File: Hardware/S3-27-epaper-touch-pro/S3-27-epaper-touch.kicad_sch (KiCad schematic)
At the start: 102 parts, among them J1 AFC24-S24FIC-00, J10 Conn_01x06_Pin, J2 Conn_01x06, J3 Conn_01x06, J4 Conn_01x06_Female, J5 Groove sensor, J6 Conn_01x05_Pin, J7 Conn_01x04_Pin, J8 Conn_01x06, Q1 Si1308, Q2 Si2301, SW1 SW_Push, SW2 SW_Push, SW3 SW_Push, SW4 SW_Push, SW5 SW_Push, SW6 SW_Push, SW7 SW_Push, SW8 SW_Push, SW9 SW_Push, U1 ESP32-S3-WROOM-1-N8, U2 RT9013, U3 KoreanHropartsElecTYPE-C-31-M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, U5 BME680, U6 TPL5110, U7 RFM95W-868S2, U8 LSM6DSL

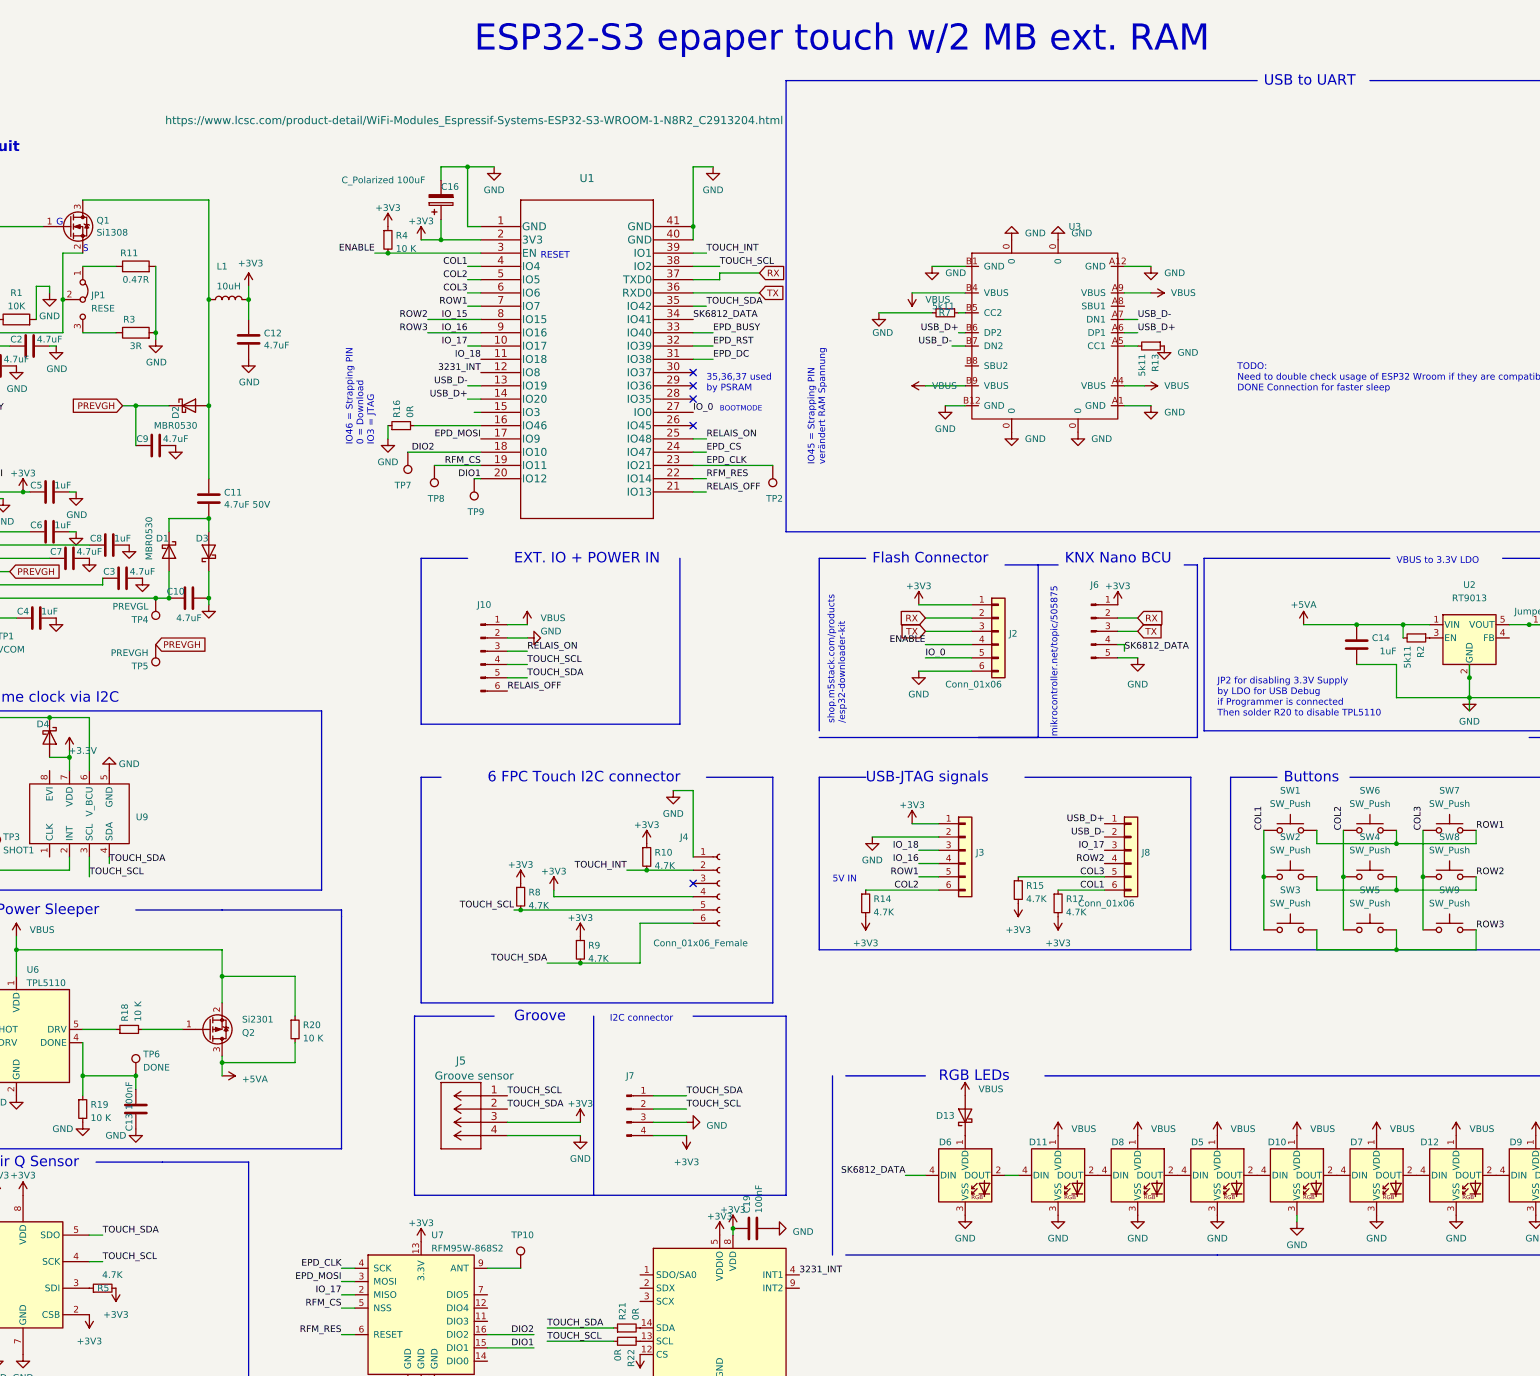
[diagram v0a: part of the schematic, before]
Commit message: Changed Footprint of BME680 and Silkscreen
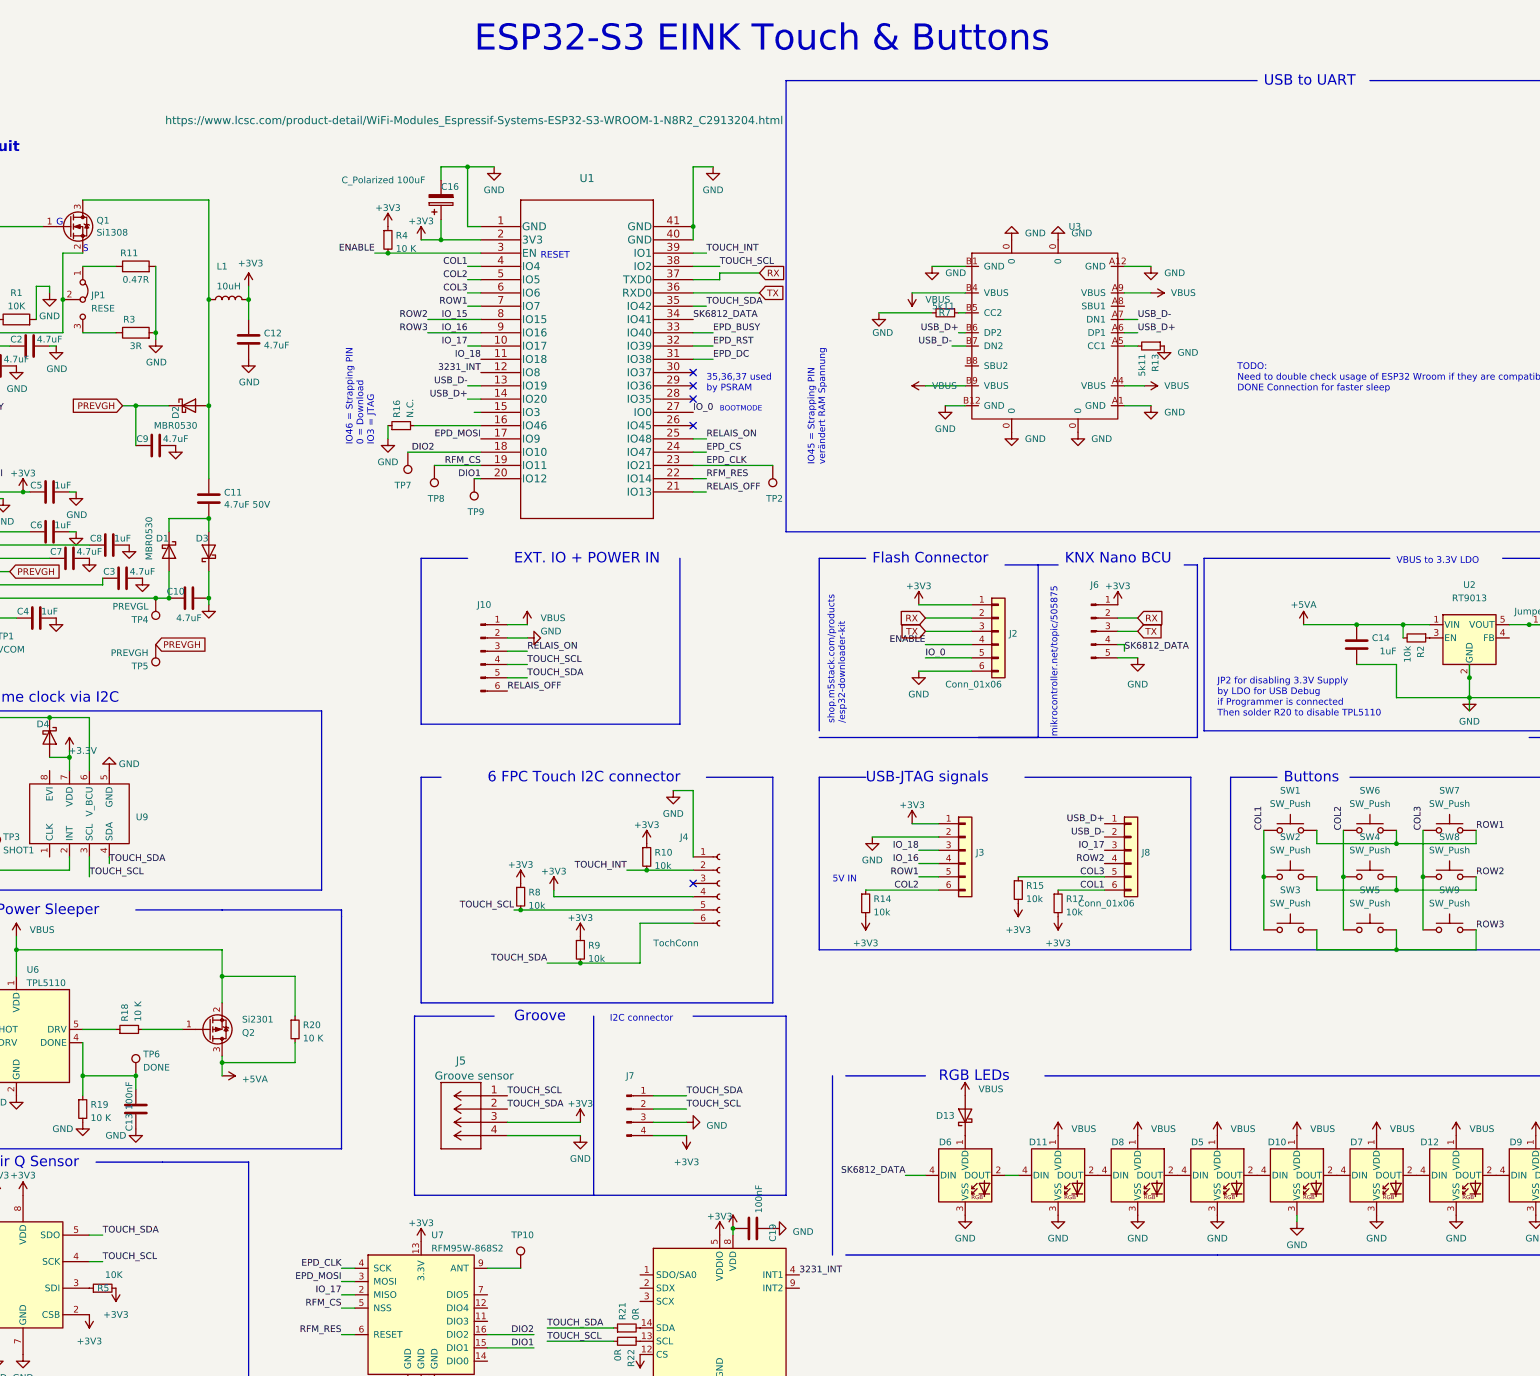
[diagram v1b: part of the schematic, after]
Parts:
- C11: LCSC C1779 -> C28323
- C13, C20: LCSC C28323 -> C49678
- C14, C15: footprint Capacitor_SMD:C_0805_2012Metric -> Capacitor_SMD:C_0805_2012Metric_Pad1.18x1.45mm_HandSolder
- C16: LCSC C129289 -> C28323
- J4: value Conn_01x06_Female -> TochConn
- L1: footprint footprint:SWPA4030S1R0NT -> tp4056:IND-SMD_L4.0-W4.0
- R10, R9: value 4.7K -> 10k; LCSC (none) -> C17414
- R12, R18, R19, R20, R4, R6: LCSC C25804 -> C17414
- R13, R7: LCSC C60816 -> C27834
- R14, R15, R17, R8: value 4.7K -> 10k; LCSC C23162 -> C17414
- R16: value 0R -> N.C.
- R2: value 5k11 -> 10k; LCSC C60816 -> C17414
- R21, R22: LCSC (none) -> C17477
- R5: value 4.7K -> 10K; LCSC C23162 -> C17414
- U5: footprint Package_LGA:Bosch_LGA-8_3x3mm_P0.8mm_ClockwisePinNumbering -> tp4056:LGA-8_L3.0-W3.0-P0.80-TR
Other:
- note added: "ESP32-S3 EINK Touch & Buttons"
- note removed: "ESP32-S3 epaper touch w/2 MB ext. RAM"
- title: ESP32-C3 epaper controller with touch -> ESP32-S3 EInk controller with touch
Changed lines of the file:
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@@
   (paper "A3")
   (title_block
-    (title "ESP32-C3 epaper controller with touch")
-    (date "2022-11-22")
-    (rev "1.1")
+    (title "ESP32-S3 EInk controller with touch")
+    (date "2023-03-07")
+    (rev "1.0")
     (comment 1 "be used in home appliances with no more than 200 Watts top consumption.")
     (comment 2 "industrial heavy load devices. This an experimental switch that should only")
     (comment 3 "it should NOT be used in any case for machinery that is for medical use or")
     (comment 4 "IMPORTANT: If used as an ON / OFF switch")
+    (comment 5 "NO Comercial USE. GPL LICENSE")
   )
   (junction (at 341.63 179.07) (diameter 0) (color 0 0 0 0)
@@
     (effects (font (size 1.27 1.27)) (justify left bottom))
   )
-  (text "ESP32-S3 epaper touch w/2 MB ext. RAM" (at 160.02 21.59 0)
+  (text "ESP32-S3 EINK Touch & Buttons" (at 160.02 21.59 0)
     (effects (font (size 5 5)) (justify left bottom))
   )
@@
       (effects (font (size 1.27 1.27)) (justify left))
     )
-    (property "Value" "4.7K" (at 170.4086 184.5822 0)
+    (property "Value" "10k" (at 170.4086 184.5822 0)
       (effects (font (size 1.27 1.27)) (justify left))
     )
@@
       (effects (font (size 1.27 1.27)) hide)
     )
-    (property "LCSC" "C23162" (at 168.91 182.88 0)
+    (property "LCSC" "C17414" (at 168.91 182.88 0)
       (effects (font (size 1.27 1.27)) hide)
     )
@@
       (effects (font (size 1.27 1.27)) hide)
     )
-    (property "LCSC" "" (at 189.23 265.43 0)
+    (property "LCSC" "C17477" (at 189.23 265.43 0)
       (effects (font (size 1.27 1.27)) hide)
     )
@@
       (effects (font (size 1.27 1.27)) hide)
     )
-    (property "LCSC" "C60816" (at 289.56 77.47 0)
+    (property "LCSC" "C27834" (at 289.56 77.47 0)
       (effects (font (size 1.27 1.27)) hide)
     )
@@
       (effects (font (size 1.27 1.27)) (justify left))
     )
-    (property "Value" "4.7K" (at 273.2786 185.8522 0)
+    (property "Value" "10k" (at 273.2786 185.8522 0)
       (effects (font (size 1.27 1.27)) (justify left))
     )
@@
       (effects (font (size 1.27 1.27)) hide)
     )
-    (property "LCSC" "C23162" (at 271.78 184.15 0)
+    (property "LCSC" "C17414" (at 271.78 184.15 0)
       (effects (font (size 1.27 1.27)) hide)
     )
@@
       (effects (font (size 1.27 1.27)) (justify left))
     )
-    (property "Value" "4.7K" (at 181.8386 194.7422 0)
+    (property "Value" "10k" (at 181.8386 194.7422 0)
       (effects (font (size 1.27 1.27)) (justify left))
     )
@@
       (effects (font (size 1.27 1.27)) hide)
     )
-    (property "LCSC" "" (at 180.34 193.04 0)
+    (property "LCSC" "C17414" (at 180.34 193.04 0)
       (effects (font (size 1.27 1.27)) hide)
     )
@@
       (effects (font (size 1.27 1.27)) (justify left))
     )
-    (property "Value" "4.7K" (at 194.5386 176.9622 0)
+    (property "Value" "10k" (at 194.5386 176.9622 0)
       (effects (font (size 1.27 1.27)) (justify left))
     )
@@
       (effects (font (size 1.27 1.27)) hide)
     )
-    (property "LCSC" "" (at 193.04 175.26 0)
+    (property "LCSC" "C17414" (at 193.04 175.26 0)
       (effects (font (size 1.27 1.27)) hide)
     )
@@
       (effects (font (size 1.27 1.27)) hide)
     )
-    (property "LCSC" "" (at 189.23 267.97 0)
+    (property "LCSC" "C17477" (at 189.23 267.97 0)
       (effects (font (size 1.27 1.27)) hide)
     )
@@
       (effects (font (size 1.27 1.27)) (justify left))
     )
-    (property "Value" "4.7K" (at 236.4486 185.8522 0)
+    (property "Value" "10k" (at 236.4486 185.8522 0)
       (effects (font (size 1.27 1.27)) (justify left))
     )
@@
       (effects (font (size 1.27 1.27)) hide)
     )
-    (property "LCSC" "C23162" (at 234.95 184.15 0)
+    (property "LCSC" "C17414" (at 234.95 184.15 0)
       (effects (font (size 1.27 1.27)) hide)
     )
@@
   (symbol (lib_id "Device:C") (at 213.36 246.38 270) (unit 1)
     (in_bom yes) (on_board yes) (dnp no)
-    (property "Reference" "C19" (at 212.1916 243.459 0)
+    (property "Reference" "C19" (at 217.17 248.92 0)
       (effects (font (size 1.27 1.27)) (justify right))
     )
@@
       (effects (font (size 1.27 1.27)) (justify right))
     )
-    (property "Footprint" "Package_LGA:Bosch_LGA-8_3x3mm_P0.8mm_ClockwisePinNumbering" (at 107.95 266.7 0)
+    (property "Footprint" "tp4056:LGA-8_L3.0-W3.0-P0.80-TR" (at 107.95 266.7 0)
       (effects (font (size 1.27 1.27)) hide)
     )
@@
       (effects (font (size 1.27 1.27)) (justify right))
     )
-    (property "Footprint" "Capacitor_SMD:C_0805_2012Metric" (at 329.8952 138.43 0)
+    (property "Footprint" "Capacitor_SMD:C_0805_2012Metric_Pad1.18x1.45mm_HandSolder" (at 329.8952 138.43 0)
       (effects (font (size 1.27 1.27)) hide)
     )
@@
       (effects (font (size 1.27 1.27)) hide)
     )
-    (property "LCSC" "C25804" (at 125.73 208.28 0)
+    (property "LCSC" "C17414" (at 125.73 208.28 0)
       (effects (font (size 1.27 1.27)) hide)
     )
@@
       (effects (font (size 1.27 1.27)) hide)
     )
-    (property "LCSC" "C25804" (at 59.69 168.91 0)
+    (property "LCSC" "C17414" (at 59.69 168.91 0)
       (effects (font (size 1.27 1.27)) hide)
     )
@@
       (effects (font (size 1.27 1.27)) hide)
     )
-    (property "LCSC" "C25804" (at 49.53 213.36 0)
+    (property "LCSC" "C17414" (at 49.53 213.36 0)
       (effects (font (size 1.27 1.27)) hide)
     )
@@
       (effects (font (size 1.27 1.27)) hide)
     )
-    (property "LCSC" "C25804" (at 93.98 208.28 0)
+    (property "LCSC" "C17414" (at 93.98 208.28 0)
       (effects (font (size 1.27 1.27)) hide)
     )
@@
       (effects (font (size 1.27 1.27)) hide)
     )
-    (property "LCSC" "C28323" (at 95.25 223.52 90)
+    (property "LCSC" "C49678" (at 95.25 223.52 90)
       (effects (font (size 1.27 1.27)) hide)
     )
@@
       (effects (font (size 1.27 1.27)) hide)
     )
-    (property "LCSC" "C129289" (at 153.67 49.53 0)
+    (property "LCSC" "C28323" (at 153.67 49.53 0)
       (effects (font (size 1.27 1.27)) hide)
     )
@@
       (effects (font (size 1.27 1.27)))
     )
-    (property "Footprint" "footprint:SWPA4030S1R0NT" (at 113.03 68.58 0)
+    (property "Footprint" "tp4056:IND-SMD_L4.0-W4.0" (at 113.03 68.58 0)
       (effects (font (size 1.27 1.27)) hide)
     )
@@
       (effects (font (size 1.27 1.27)) (justify right))
     )
-    (property "Footprint" "Capacitor_SMD:C_0805_2012Metric" (at 371.8052 142.24 0)
+    (property "Footprint" "Capacitor_SMD:C_0805_2012Metric_Pad1.18x1.45mm_HandSolder" (at 371.8052 142.24 0)
       (effects (font (size 1.27 1.27)) hide)
     )
@@
       (effects (font (size 1.27 1.27)) hide)
     )
-    (property "LCSC" "C25804" (at 143.51 57.15 0)
+    (property "LCSC" "C17414" (at 143.51 57.15 0)
       (effects (font (size 1.27 1.27)) hide)
     )
@@
       (effects (font (size 1.27 1.27)) (justify left))
     )
-    (property "Value" "5k11" (at 338.6578 134.8486 0)
+    (property "Value" "10k" (at 338.6578 134.8486 0)
       (effects (font (size 1.27 1.27)) (justify left))
     )
@@
       (effects (font (size 1.27 1.27)) hide)
     )
-    (property "LCSC" "C60816" (at 340.36 133.35 0)
+    (property "LCSC" "C17414" (at 340.36 133.35 0)
       (effects (font (size 1.27 1.27)) hide)
     )
@@
       (effects (font (size 1.27 1.27)) (justify left))
     )
-    (property "Value" "0R" (at 147.7522 91.2114 0)
+    (property "Value" "N.C." (at 147.7522 91.2114 0)
       (effects (font (size 1.27 1.27)) (justify left))
     )
@@
       (effects (font (size 1.27 1.27)) (justify left))
     )
-    (property "Value" "Conn_01x06_Female" (at 194.31 191.77 0)
+    (property "Value" "TochConn" (at 194.31 191.77 0)
       (effects (font (size 1.27 1.27)) (justify left))
     )
@@
       (effects (font (size 1.27 1.27)) hide)
     )
-    (property "LCSC" "C25804" (at 85.09 223.52 0)
+    (property "LCSC" "C17414" (at 85.09 223.52 0)
       (effects (font (size 1.27 1.27)) hide)
     )
@@
       (effects (font (size 1.27 1.27)) hide)
     )
-    (property "LCSC" "C1779" (at 109.22 106.68 0)
+    (property "LCSC" "C28323" (at 109.22 106.68 0)
       (effects (font (size 1.27 1.27)) hide)
     )
@@
     )
     (property "Value" "+3V3" (at 209.55 242.8042 0)
-      (effects (font (size 1.27 1.27)))
+      (effects (font (size 1.27 1.27)) hide)
     )
     (property "Footprint" "" (at 209.55 246.38 0)
@@
       (effects (font (size 1.27 1.27)) hide)
     )
-    (property "LCSC" "C28323" (at 62.23 241.3 90)
+    (property "LCSC" "C49678" (at 62.23 241.3 90)
       (effects (font (size 1.27 1.27)) hide)
     )
@@
       (effects (font (size 1.27 1.27)) (justify left))
     )
-    (property "Value" "4.7K" (at 92.71 255.27 90)
+    (property "Value" "10K" (at 92.71 255.27 90)
       (effects (font (size 1.27 1.27)) (justify left))
     )
@@
       (effects (font (size 1.27 1.27)) hide)
     )
-    (property "LCSC" "C23162" (at 88.9 257.81 0)
+    (property "LCSC" "C17414" (at 88.9 257.81 0)
       (effects (font (size 1.27 1.27)) hide)
     )
@@
       (effects (font (size 1.27 1.27)) hide)
     )
-    (property "LCSC" "C60816" (at 250.19 71.12 0)
+    (property "LCSC" "C27834" (at 250.19 71.12 0)
       (effects (font (size 1.27 1.27)) hide)
     )
@@
       (effects (font (size 1.27 1.27)) (justify left))
     )
-    (property "Value" "4.7K" (at 265.6586 183.3122 0)
+    (property "Value" "10k" (at 265.6586 183.3122 0)
       (effects (font (size 1.27 1.27)) (justify left))
     )
@@
       (effects (font (size 1.27 1.27)) hide)
     )
-    (property "LCSC" "C23162" (at 264.16 181.61 0)
+    (property "LCSC" "C17414" (at 264.16 181.61 0)
       (effects (font (size 1.27 1.27)) hide)
     )
